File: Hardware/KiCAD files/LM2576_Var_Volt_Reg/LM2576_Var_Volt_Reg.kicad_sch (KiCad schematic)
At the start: 14 parts, among them J1 Conn_01x03_Pin, U2 LM2576HVS-ADJ

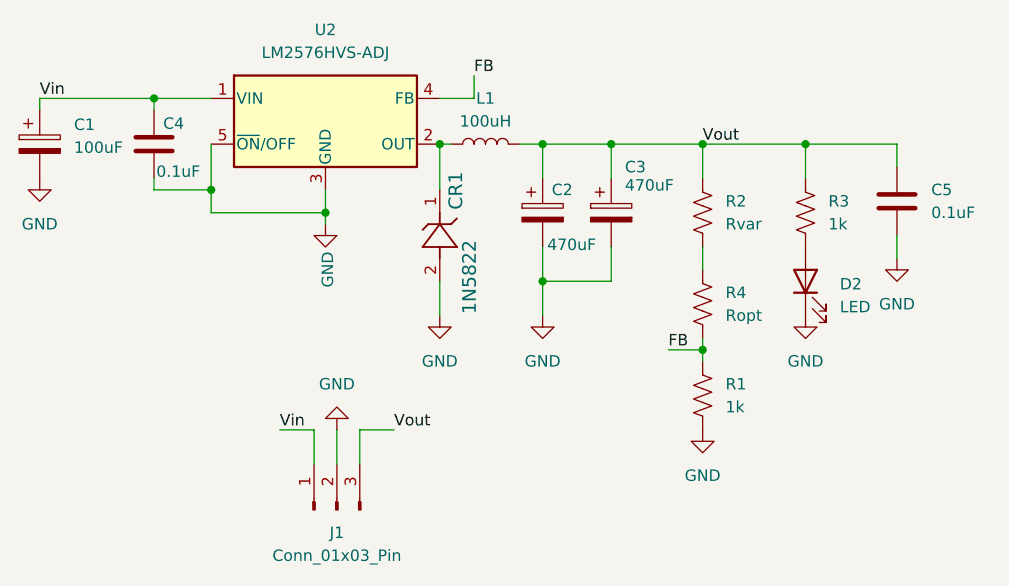
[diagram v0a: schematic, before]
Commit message: 1st push of PCB's for printing
This is pre-peer review. This almost certainly has section that need adjustment. also realized I'm missing the USB-Uart bridge. first thing added in next version.
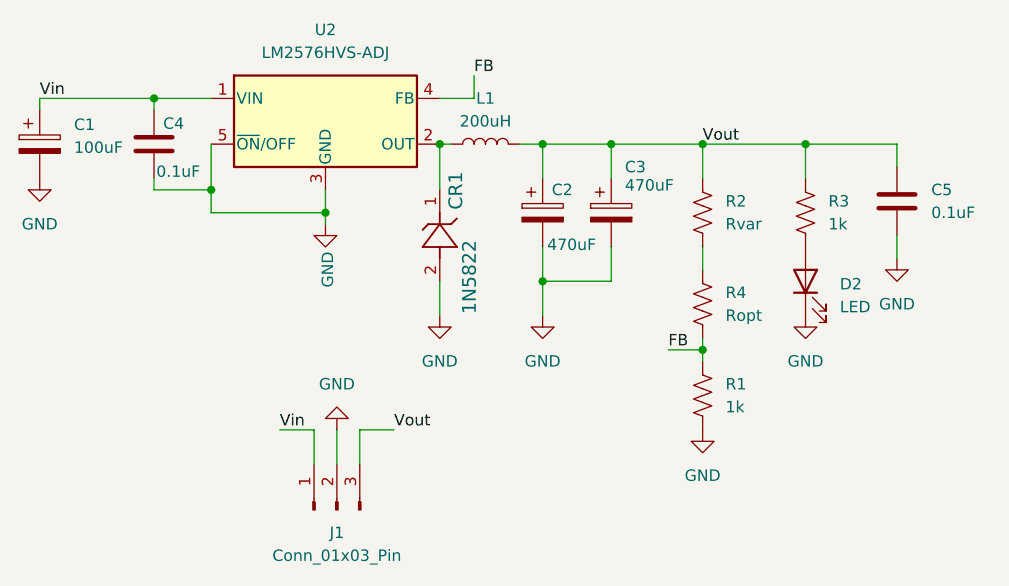
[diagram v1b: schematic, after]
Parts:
- L1: value 100uH -> 200uH

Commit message: general progress and adjustments
new footprint for pi reg inductor, var reg checked concurred with current part and value. re footprinted motor driver. started swapping head. adjusted some device footprints.
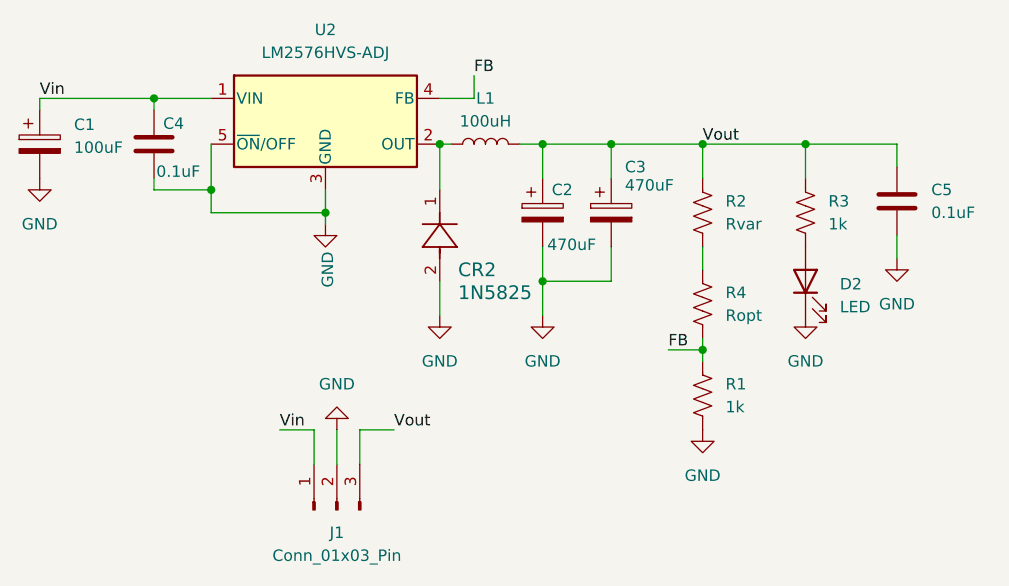
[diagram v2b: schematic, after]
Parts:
- removed CR1: 1N5822, 1N5822:DO-201AD_STM, symbol 1N5822:1N5822
- added CR2: 1N5825, 1N5825_MCH, symbol 2026-04-06_22-20-55:1N5825
- L1: value 200uH -> 100uH
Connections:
- net GND: now also CR2.2
- net at L1.1, U2.2 (OUT): now also CR2.1
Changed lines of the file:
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@@
 			)
 		)
-		(property "Value" "200uH"
+		(property "Value" "100uH"
 			(at 138.43 59.69 90)
 			(show_name no)
@@
 	)
 	(symbol
-		(lib_id "1N5822:1N5822")
-		(at 133.35 67.31 270)
-		(unit 1)
-		(body_style 1)
-		(exclude_from_sim no)
-		(in_bom yes)
-		(on_board yes)
-		(in_pos_files yes)
-		(dnp no)
-		(property "Reference" "CR1"
-			(at 135.128 65.278 0)
-			(show_name no)
-			(do_not_autoplace no)
-			(effects
-				(font
-					(size 1.524 1.524)
-				)
-				(justify left)
-			)
-		)
-		(property "Value" "1N5822"
-			(at 136.652 72.898 0)
-			(show_name no)
-			(do_not_autoplace no)
-			(effects
-				(font
-					(size 1.524 1.524)
-				)
-				(justify left)
-			)
-		)
-		(property "Footprint" "1N5822:DO-201AD_STM"
-			(at 133.35 67.31 0)
-			(hide yes)
-			(show_name no)
-			(do_not_autoplace no)
-			(effects
-				(font
-					(size 1.27 1.27)
-					(italic yes)
-				)
-			)
-		)
-		(property "Datasheet" "https://www.st.com/resource/en/datasheet/1n5822.pdf"
-			(at 133.35 67.31 0)
-			(hide yes)
-			(show_name no)
-			(do_not_autoplace no)
-			(effects
-				(font
-					(size 1.27 1.27)
-					(italic yes)
-				)
-			)
-		)
-		(property "Description" ""
-			(at 133.35 67.31 0)
-			(hide yes)
-			(show_name no)
-			(do_not_autoplace no)
-			(effects
-				(font
-					(size 1.27 1.27)
-				)
-			)
-		)
-		(pin "1"
-		)
-		(pin "2"
-		)
-		(instances
-			(project "LM2576_Var_Volt_Reg"
-				(path "/05ad55a9-73a4-4419-8d6d-9b068d5aca56"
-					(reference "CR1")
-					(unit 1)
-				)
-			)
-		)
-	)
-	(symbol
 		(lib_id "Device:C_Polarized")
 		(at 144.78 69.85 0)
@@
 					(unit 1)
 				)
+			)
+		)
+	)
+	(symbol
+		(lib_id "2026-04-06_22-20-55:1N5825")
+		(at 133.35 77.47 90)
+		(unit 1)
+		(body_style 1)
+		(exclude_from_sim no)
+		(in_bom yes)
+		(on_board yes)
+		(in_pos_files yes)
+		(dnp no)
+		(property "Reference" "CR2"
+			(at 135.382 76.2 90)
+			(show_name no)
+			(do_not_autoplace no)
+			(effects
+				(font
+					(size 1.524 1.524)
+				)
+				(justify right)
+			)
+		)
+		(property "Value" "1N5825"
+			(at 135.382 78.74 90)
+			(show_name no)
+			(do_not_autoplace no)
+			(effects
+				(font
+					(size 1.524 1.524)
+				)
+				(justify right)
+			)
+		)
+		(property "Footprint" "1N5825_MCH"
+			(at 133.35 77.47 0)
+			(hide yes)
+			(show_name no)
+			(do_not_autoplace no)
+			(effects
+				(font
+					(size 1.27 1.27)
+					(italic yes)
+				)
+			)
+		)
+		(property "Datasheet" "1N5825"
+			(at 133.35 77.47 0)
+			(hide yes)
+			(show_name no)
+			(do_not_autoplace no)
+			(effects
+				(font
+					(size 1.27 1.27)
+					(italic yes)
+				)
+			)
+		)
+		(property "Description" ""
+			(at 133.35 77.47 0)
+			(hide yes)
+			(show_name no)
+			(do_not_autoplace no)
+			(effects
+				(font
+					(size 1.27 1.27)
+				)
+			)
+		)
+		(pin "1"
+		)
+		(pin "2"
+		)
+		(instances
+			(project "LM2576_Var_Volt_Reg"
+				(path "/05ad55a9-73a4-4419-8d6d-9b068d5aca56"
+					(reference "CR2")
+					(unit 1)
+				)
